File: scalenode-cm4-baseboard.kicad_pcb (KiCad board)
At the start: 4 copper layers, 128.5 x 40 mm, 148 parts, among them IC1 TPS2378DDA, J1 B2B-XH-A_LF__SN_, J10 LSHM-130-01-L-RH-A-S-K-TR, J3 1-2199230-6, J4 1140084168, J5 0473460001, J6 SS-74800-144, J7 DF40HC(3.0)-100DS-0.4v, J8 DF40HC(3.0)-100DS-0.4v, Q6 BSS138-7-F, U1 TS3USB30EDGSR, U2 AP62301WU-7, U3 TPS2373-3RGW, U4 URB4805YMD-30WR3, U5 TS3USB30EDGSR, U6 FT234XD-R

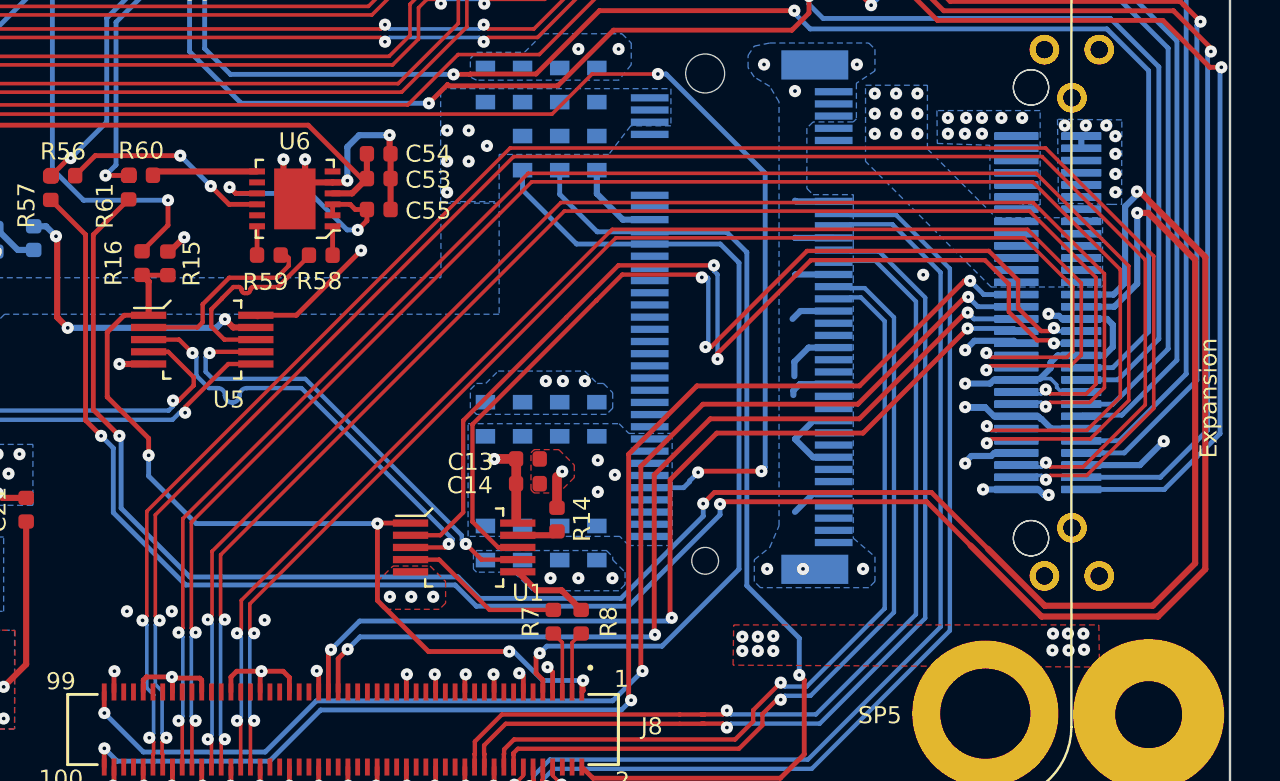
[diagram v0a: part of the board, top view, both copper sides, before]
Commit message: Tune hdmi0 tracks
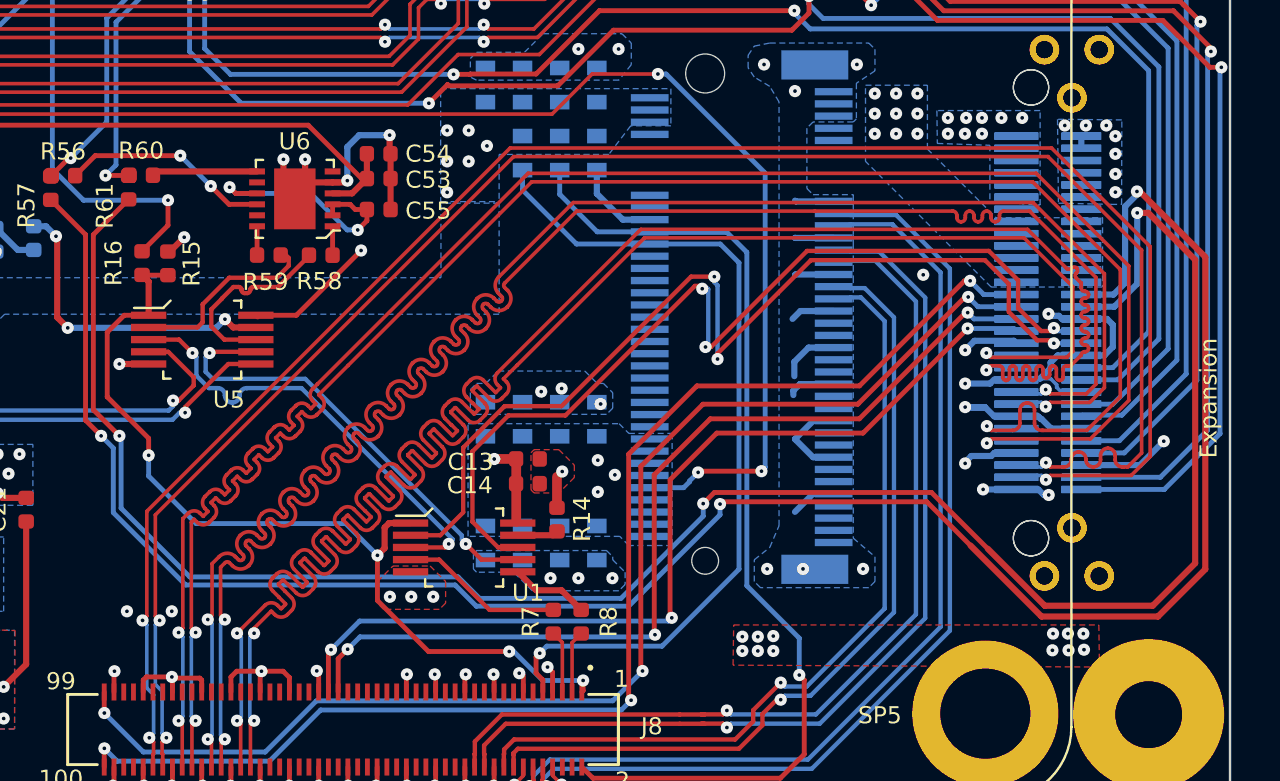
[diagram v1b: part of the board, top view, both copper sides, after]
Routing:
- net HDMI0_D2_N: track 57.3 -> 83.0 mm
- net HDMI0_D2_P: track 55.5 -> 74.3 mm
- net HDMI0_D1_P: track 59.9 -> 73.9 mm
- net HDMI0_D1_N: track 61.6 -> 74.0 mm
- net HDMI0_D0_P: track 68.4 -> 74.4 mm
- net HDMI0_D0_N: track 71.0 -> 75.3 mm
- net HDMI0_CK_P: track 71.7 -> 74.4 mm
- net Adapter_USB_P: track 42.1 -> 40.8 mm
- net Adapter_USB_N: track 40.6 -> 39.3 mm
- net HDMI0_CK_N: track 73.4 -> 74.5 mm
- net GND: vias 129 -> 128

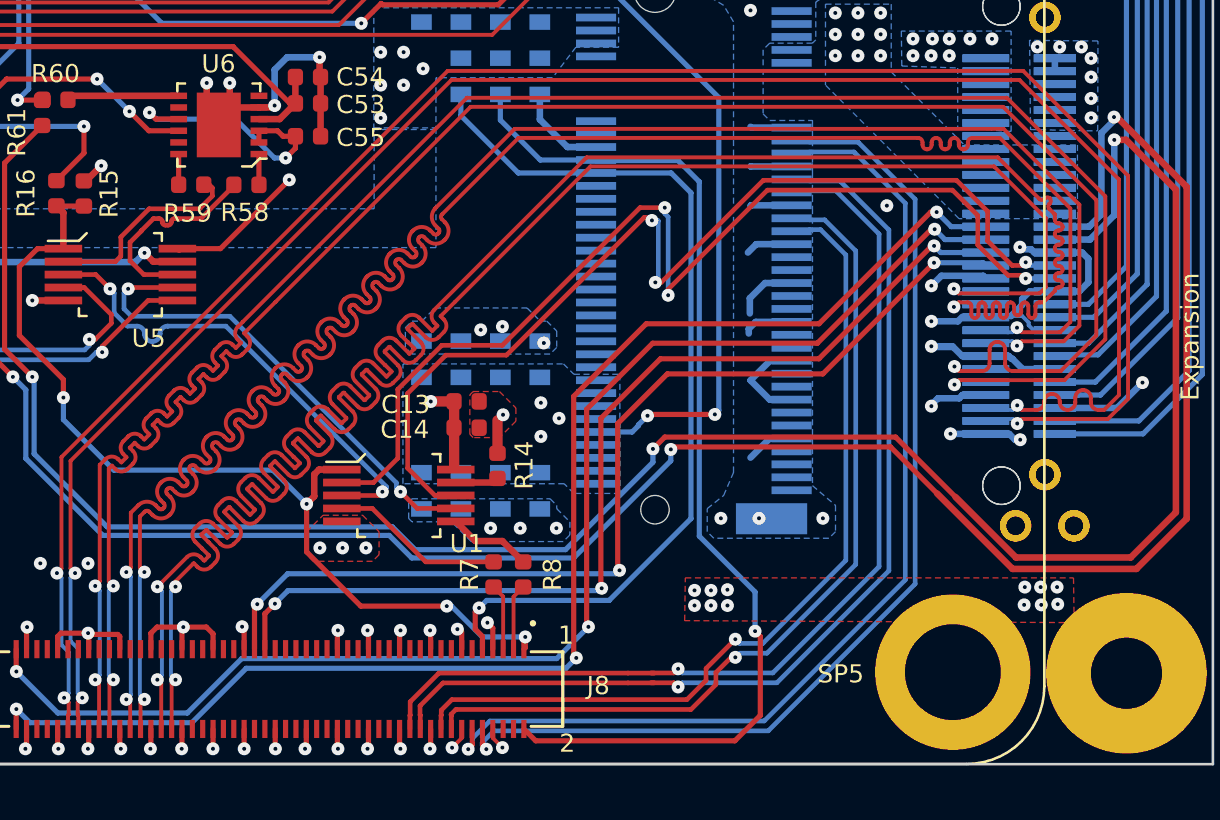
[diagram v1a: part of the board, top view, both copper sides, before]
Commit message: Improve hdmi0 tuning
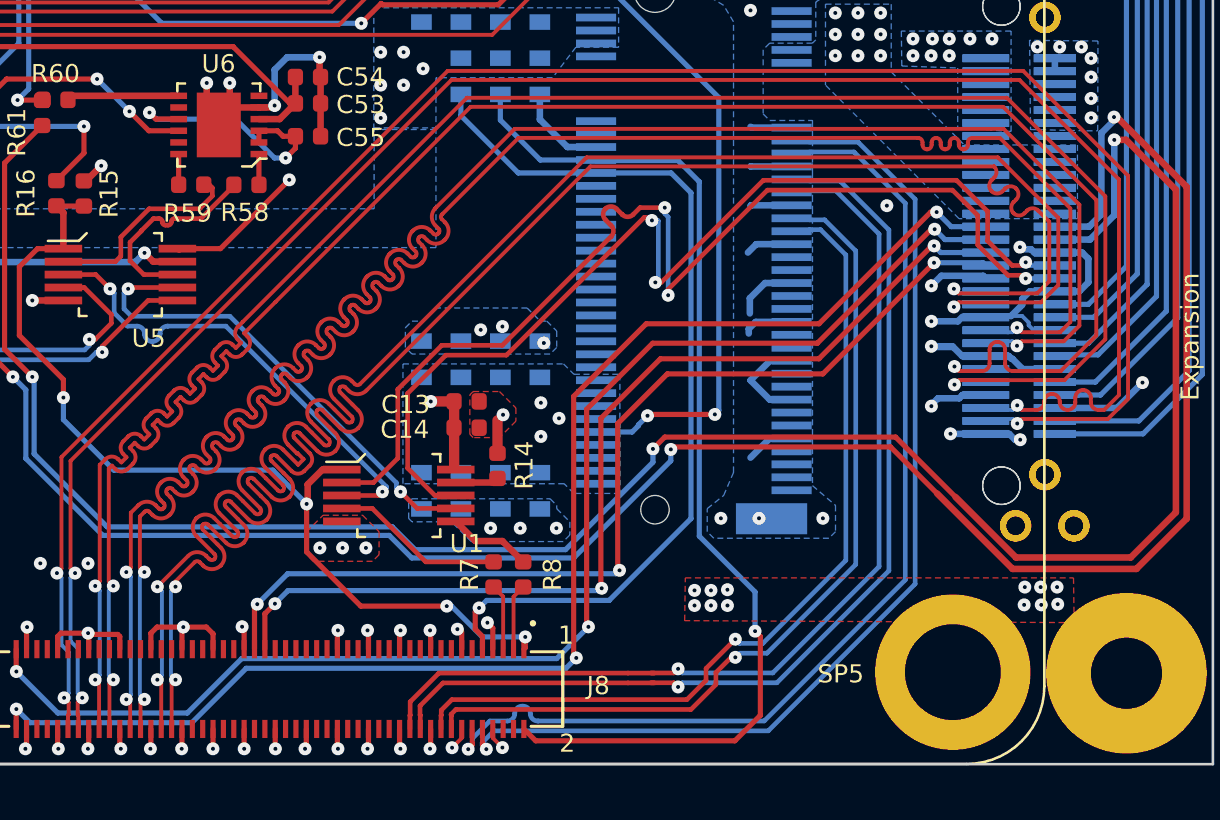
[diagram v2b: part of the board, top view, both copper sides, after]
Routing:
- net HDMI0_D2_N: track 83.0 -> 74.3 mm
- net Adapter_USB_P: track 40.8 -> 42.1 mm
- net PCIE_CLK_N: track 39.6 -> 40.3 mm

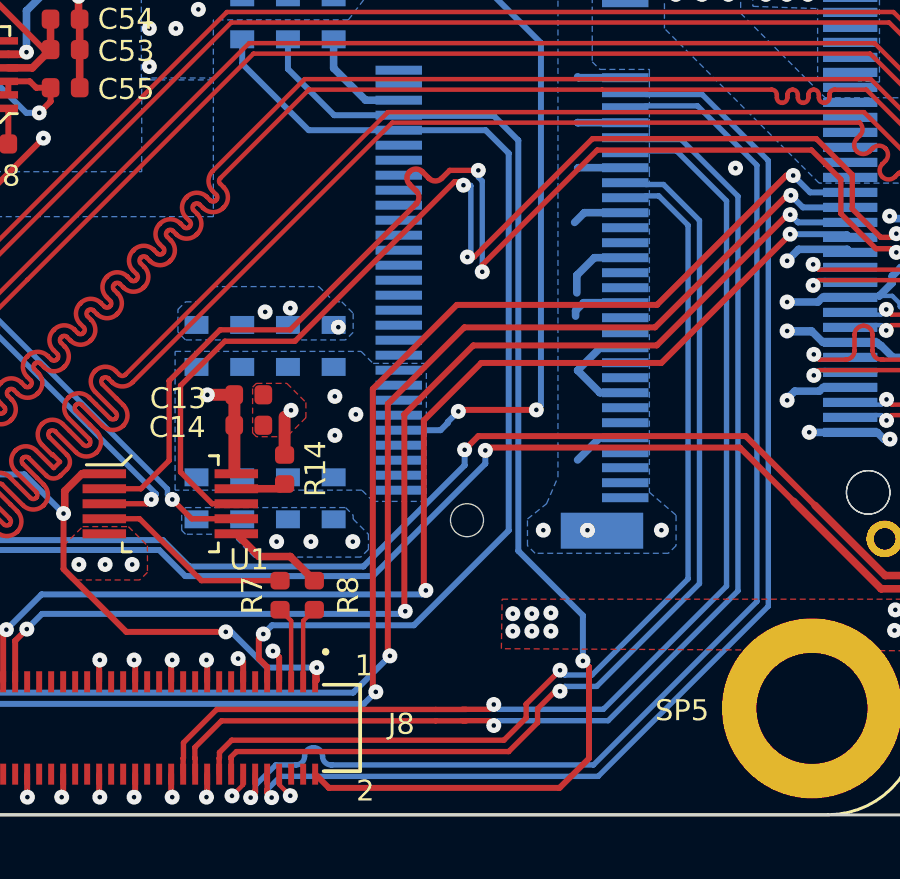
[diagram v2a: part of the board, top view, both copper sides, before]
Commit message: Tune PCIe tracks
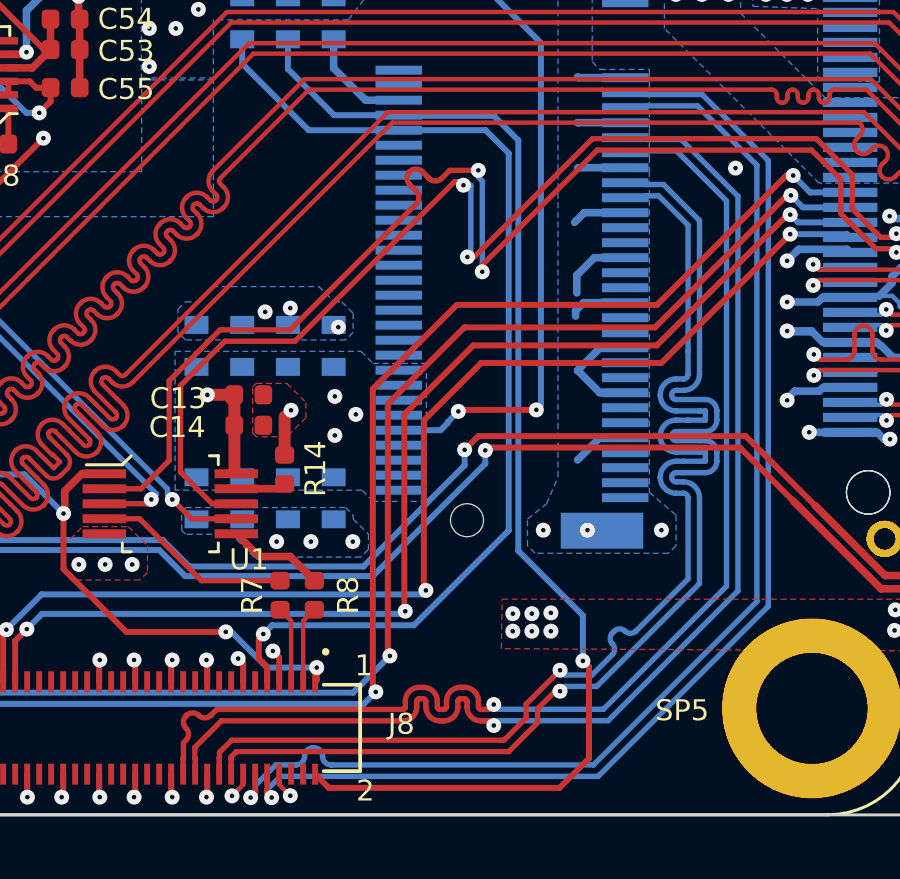
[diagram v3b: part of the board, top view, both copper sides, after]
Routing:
- net PCIE_RX_N: track 33.5 -> 40.2 mm
- net PCIE_RX_P: track 34.0 -> 40.2 mm
- net PCIE_TX_N: track 37.8 -> 40.2 mm
- net PCIE_TX_P: track 38.4 -> 40.2 mm

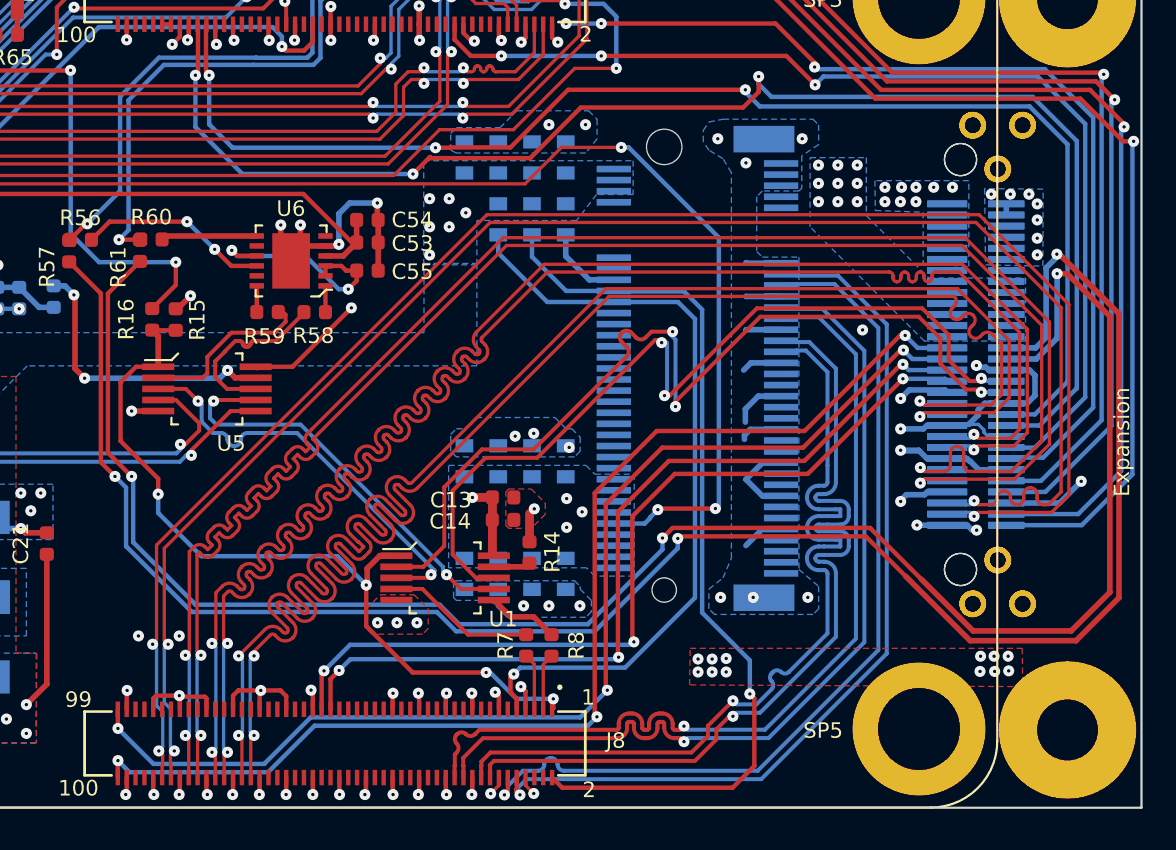
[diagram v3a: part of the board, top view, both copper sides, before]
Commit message: Relocate zones underneath differential pairs
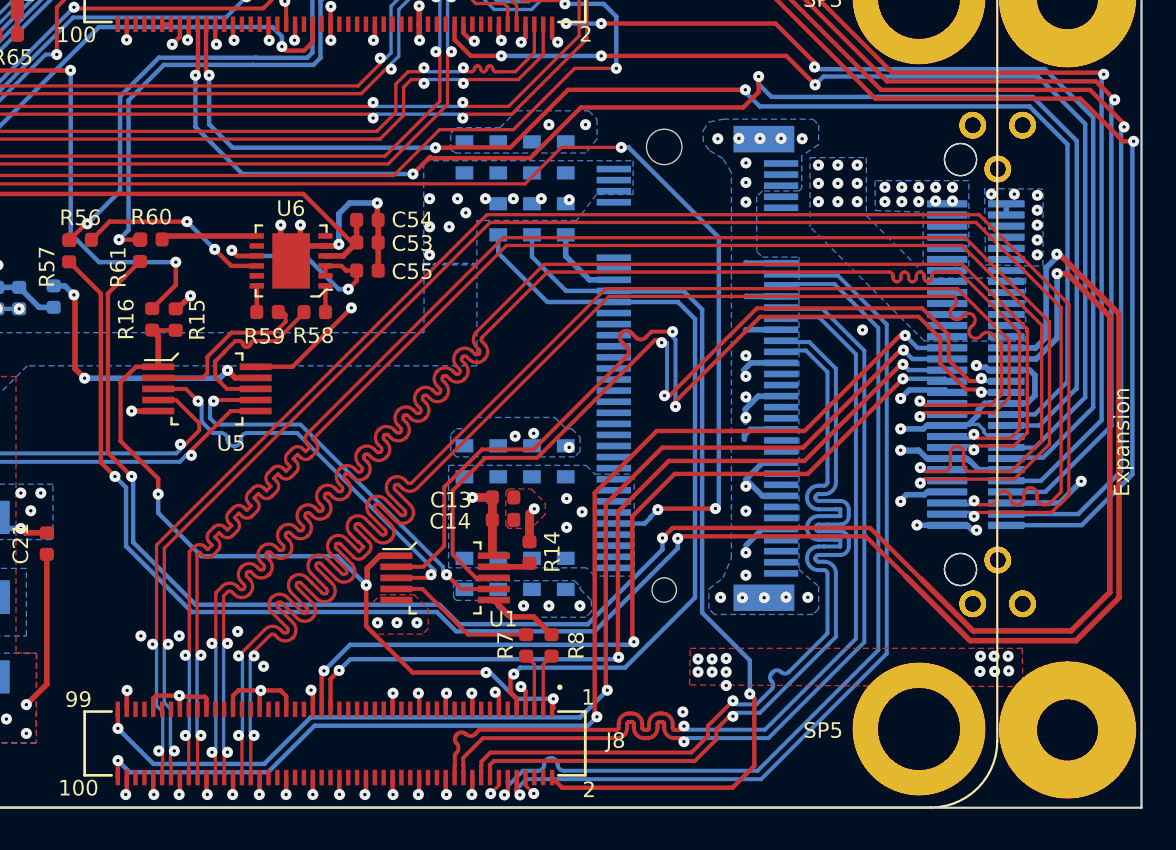
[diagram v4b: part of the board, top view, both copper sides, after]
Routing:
- net VCC5V0: vias 52 -> 54
- net GND: vias 128 -> 145
- net 3V3_SSD: vias 30 -> 34
- net 3V3_OUT: vias 26 -> 28
